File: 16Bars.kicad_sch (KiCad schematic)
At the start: 54 parts, among them IC1 CD4033BE, IC2 CD4033BE, IC3 CD4510BE, IC4 CD4510BE, IC5 CD4510BE, J1 3.5mm_Mono_Switched, J2 Conn_02x05_Odd_Even, Q1 2N3904, Q3 2N3904, Q4 2N3904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

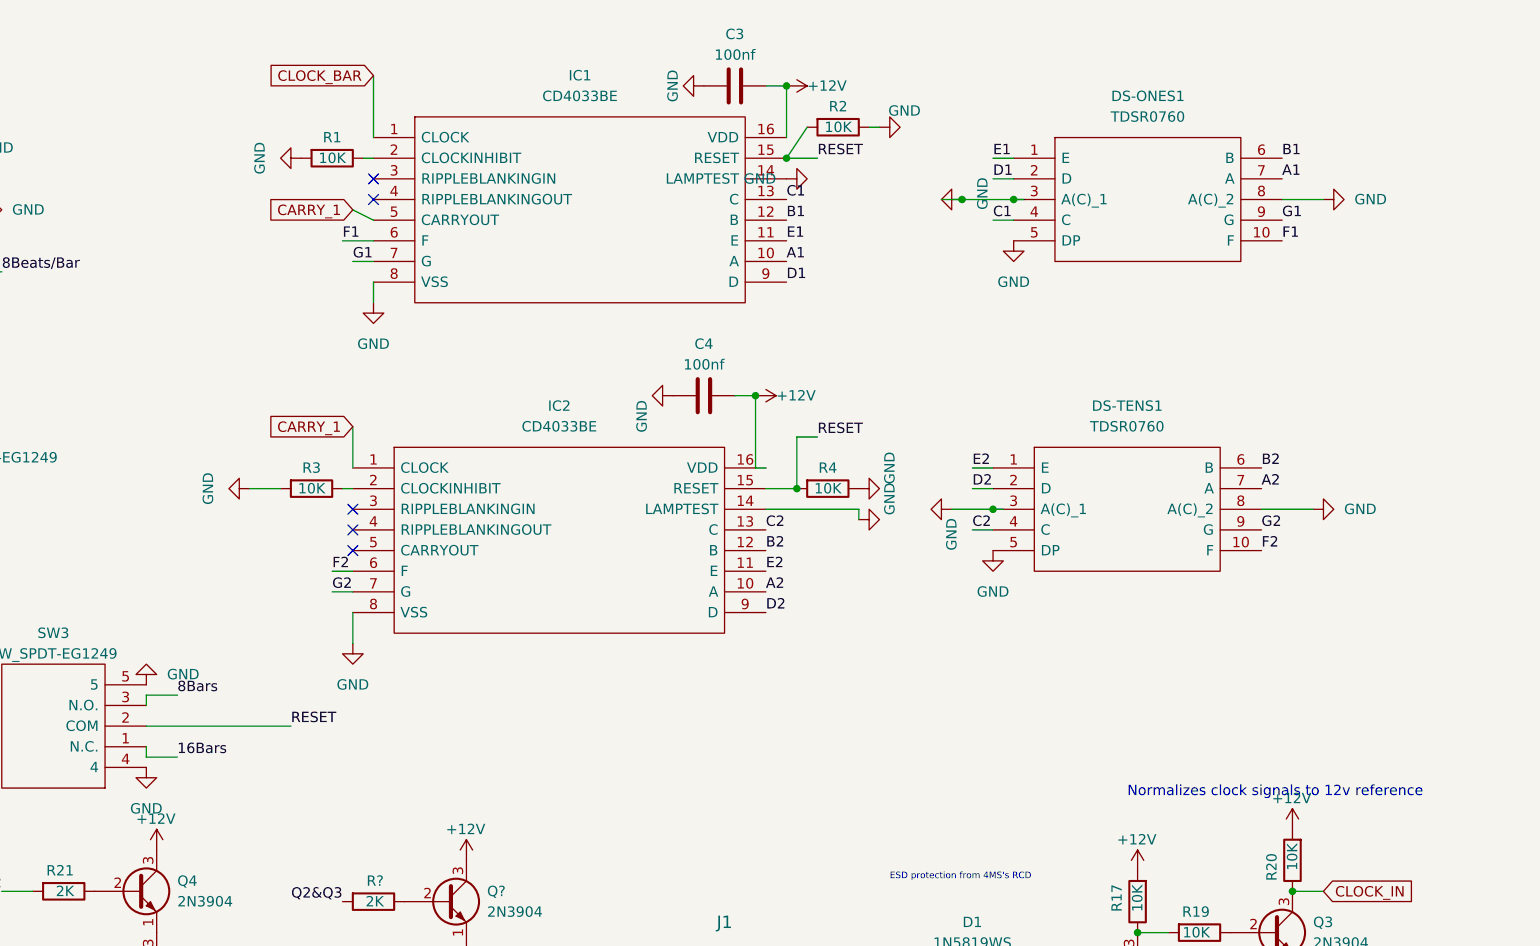
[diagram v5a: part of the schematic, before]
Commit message: Add SevenSegment sub-board
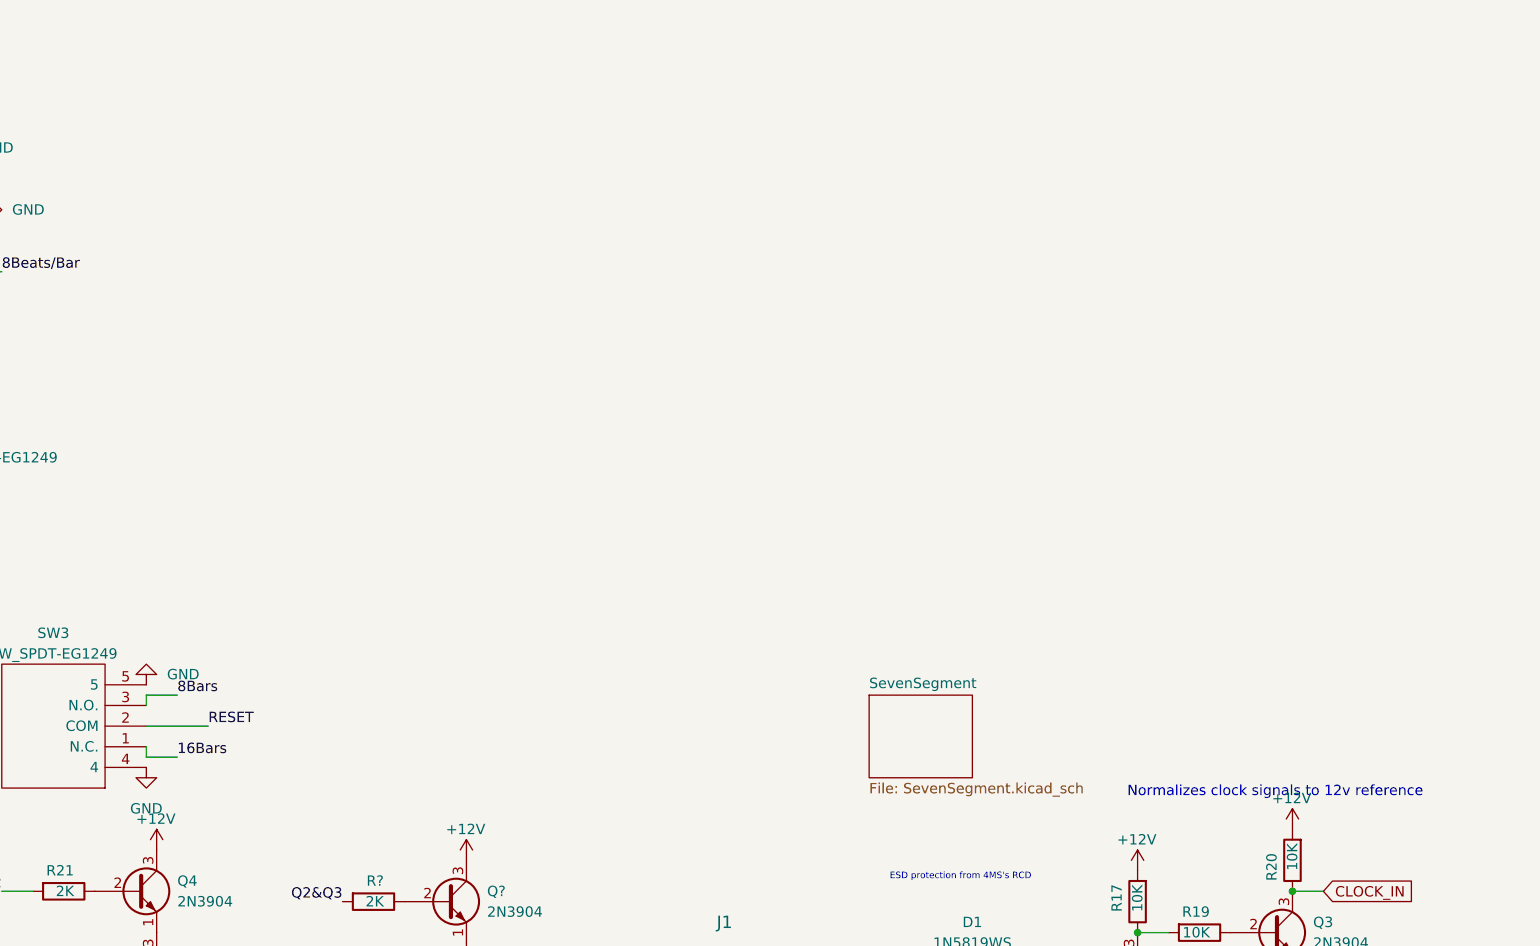
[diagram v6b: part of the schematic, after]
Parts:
- removed C3, C4: 100nf, Capacitor_SMD:C_0402_1005Metric, symbol Device:C
- removed DS-ONES1, DS-TENS1: TDSR0760, TDSR*:TDSR0760, symbol SamacSys_Parts:TDSR0760
- removed IC1, IC2: CD4033BE, DIP794W53P254L1930H508Q16N, symbol SamacSys_Parts:CD4033BE
- removed R1, R2, R3, R4: 10K, Resistor_SMD:R_0402_1005Metric, symbol Device:R
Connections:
- no-connect marks 12 -> 7
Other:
- added sheet SevenSegment (SevenSegment.kicad_sch)

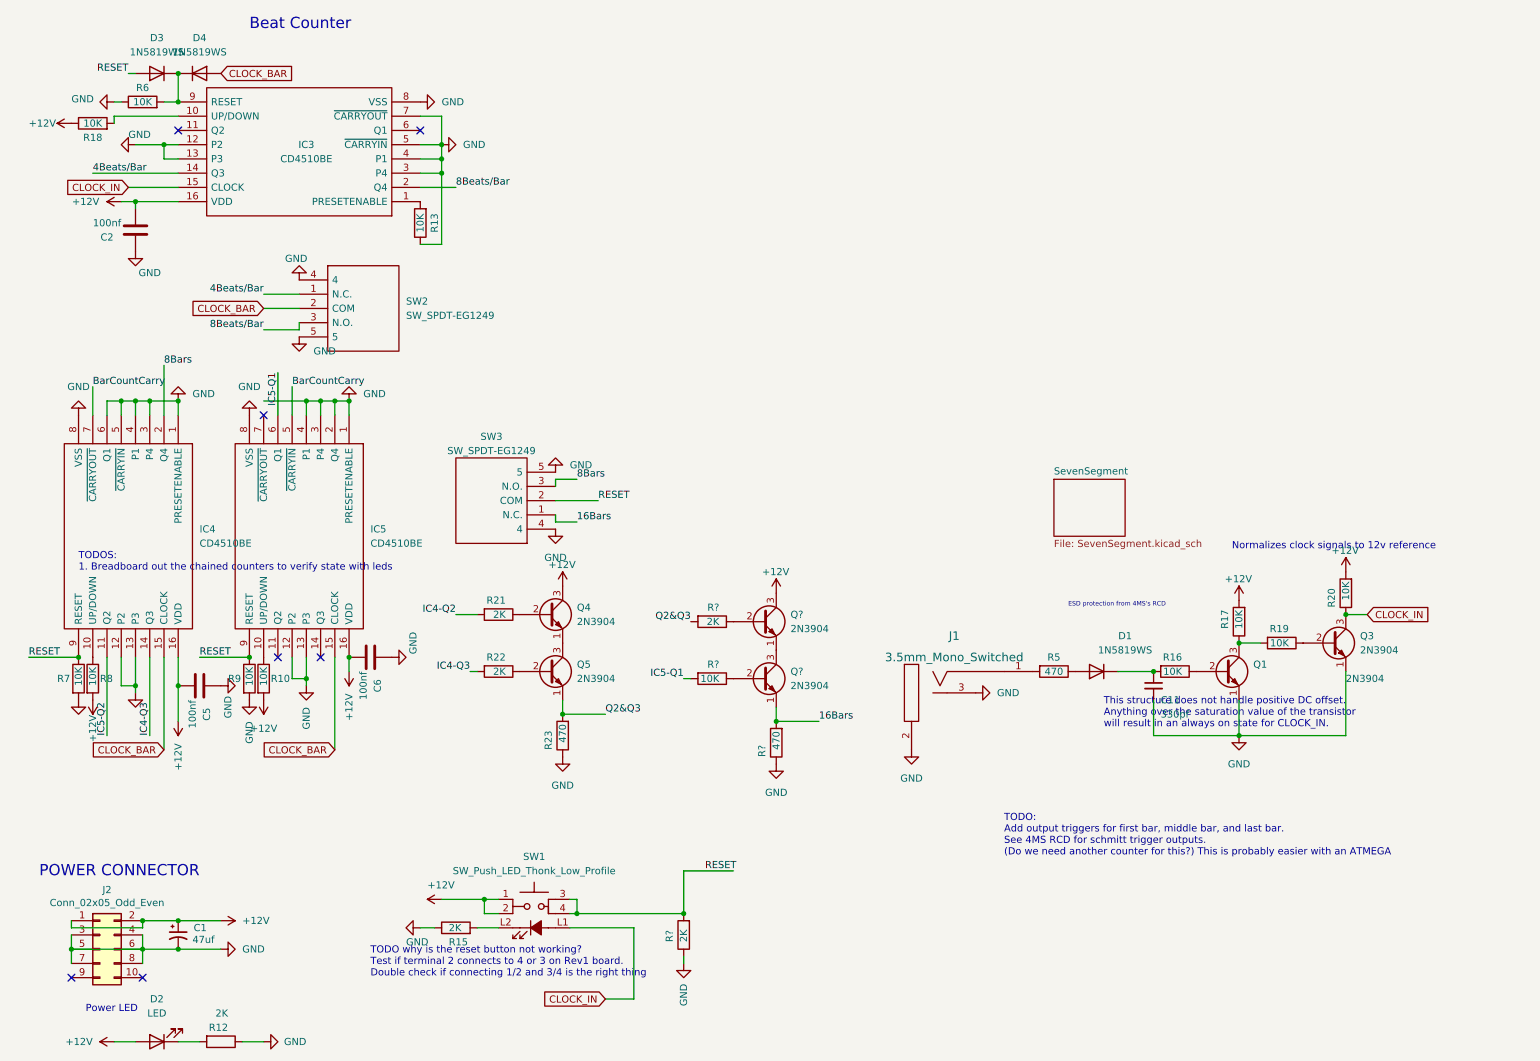
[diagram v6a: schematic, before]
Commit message: Layout SevenSegment Board. Nano Schematic
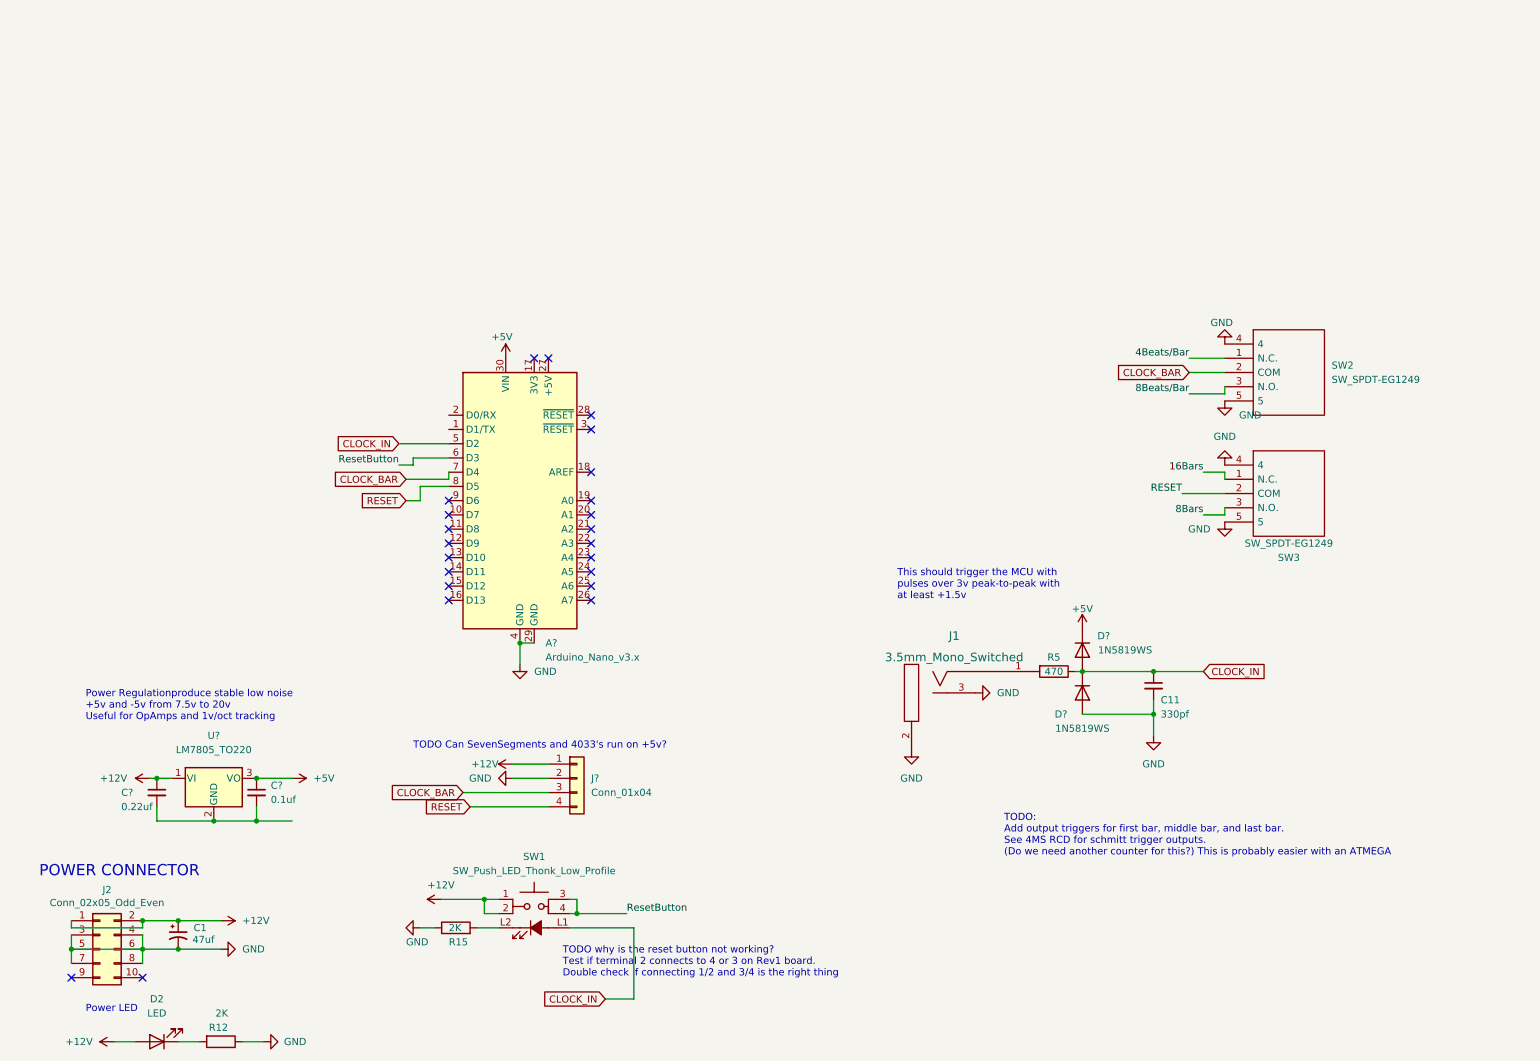
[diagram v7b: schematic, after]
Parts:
- removed C2, C5, C6: 100nf, Capacitor_SMD:C_0402_1005Metric, symbol Device:C
- removed D1, D3, D4: 1N5819WS, Diode_SMD:D_SOD-323, symbol Device:D
- removed IC3, IC4, IC5: CD4510BE, DIP794W53P254L1930H508Q16N, symbol SamacSys_Parts:CD4510BE
- removed Q1, Q3, Q4, Q5, Q? (x2): 2N3904, Package_TO_SOT_THT:TO-92_Inline, symbol Transistor_BJT:2N3904
- removed R10, R13, R16, R17, R18, R19, R20, R6, R7, R8, R9, R?: 10K, Resistor_SMD:R_0402_1005Metric, symbol Device:R
- removed R21, R22, R? (x2): 2K, Resistor_SMD:R_0402_1005Metric, symbol Device:R
- removed R23, R?: 470, Resistor_SMD:R_0402_1005Metric, symbol Device:R
- added A?: Arduino_Nano_v3.x, Module:Arduino_Nano, symbol MCU_Module:Arduino_Nano_v3.x
- added C?: 0.1uf, symbol Device:C_Small
- added C?: 0.22uf, symbol Device:C_Small
- added D? (x2): 1N5819WS, Diode_SMD:D_SOD-323, symbol Device:D
- added J?: Conn_01x04, 4ms_Connector:Pins_1x04_2.54mm_TH_SWD, symbol 4ms_Connector:Conn_01x04
- added U?: LM7805_TO220, Package_TO_SOT_THT:TO-220-3_Vertical, symbol Regulator_Linear:LM7805_TO220
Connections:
- net +12V: now also C?.1, J?.1 (Pin_1), U?.1 (VI)
- net CLOCK_BAR: now also A?.7 (D4), J?.3 (Pin_3)
- net CLOCK_IN: now also C11.1, R5.1, A?.5 (D2), D?.1 (K), D?.2 (A)
- net GND: now also A?.29 (GND), A?.4 (GND), D?.2 (A), J?.2 (Pin_2)
- net RESET: now also A?.8 (D5), J?.4 (Pin_4); no longer SW1.3, SW1.4
- new net: C?.2, C?.2, U?.2 (GND)
- new net +5V: A?.30 (VIN), C?.1, D?.1 (K), U?.3 (VO)
- new net ResetButton: A?.6 (D3), SW1.3, SW1.4
- no-connect marks 7 -> 23
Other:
- removed sheet SevenSegment
- note added: "Power Regulationproduce stable low noise +5v and -5v from 7.5v to 20v Useful for OpAmps and 1v/oct tracking"
- note added: "TODO Can SevenSegments and 4033's run on +5v?"
- note added: "This should trigger the MCU with pulses over 3v peak-to-peak with at least +1.5v"
- note removed: "Beat Counter"
- note removed: "ESD protection from 4MS's RCD"
- note removed: "Normalizes clock signals to 12v reference"
- note removed: "TODOS: 1. Breadboard out the chained counters to verify state with leds"
- note removed: "This structure does not handle positive DC offset. Anything over the saturation value of the transistor will result in an always on state for CLOCK_IN."
- moved on the sheet: SW2, SW3

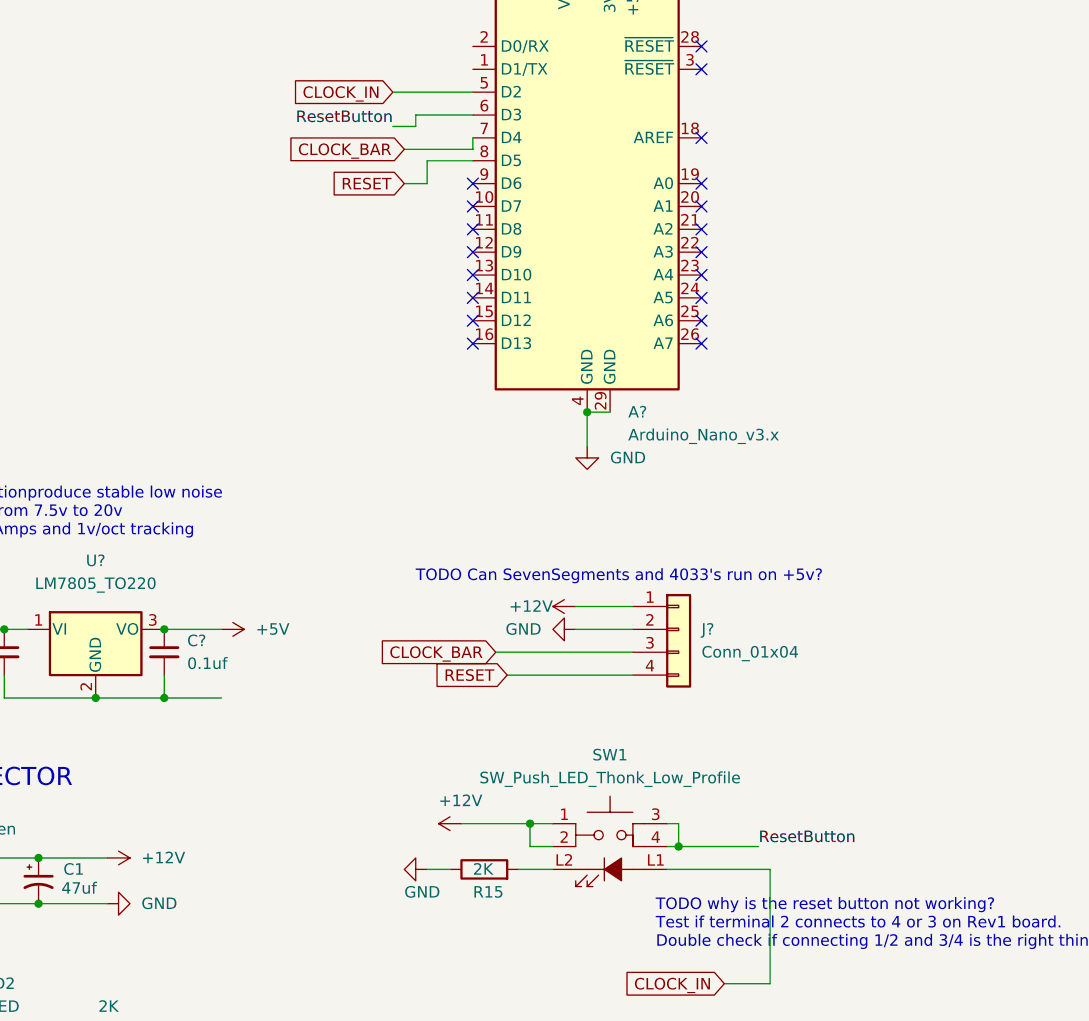
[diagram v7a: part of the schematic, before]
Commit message: Add LED output pins. Hookup pins in schematic.
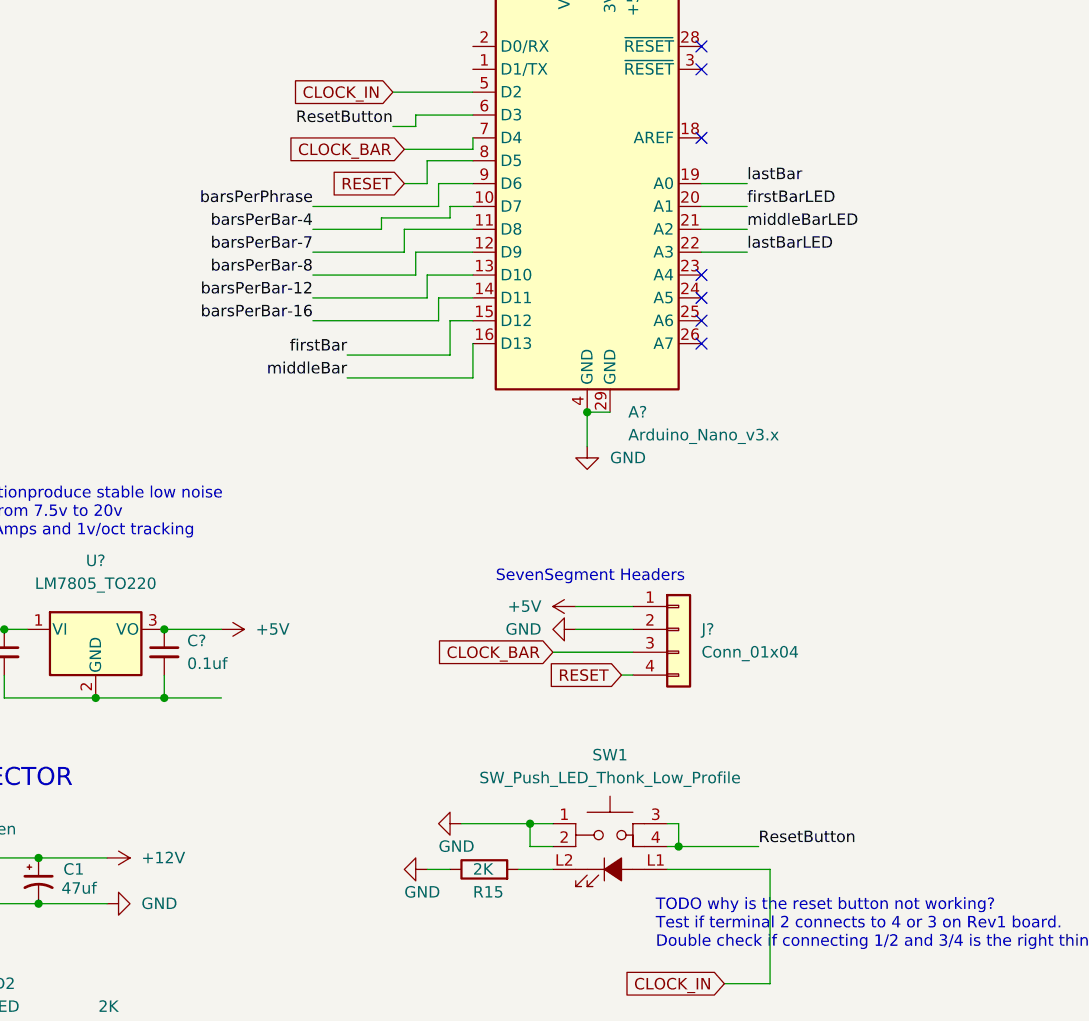
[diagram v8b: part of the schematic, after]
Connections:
- net +12V: no longer J?.1 (Pin_1), SW1.1, SW1.2
- net +5V: now also J?.1 (Pin_1)
- net GND: now also SW1.1, SW1.2
- net barsPerBar-4: now reaches A?.10 (D7)
- net barsPerBar-7: now reaches A?.11 (D8)
- net barsPerBar-8: now reaches A?.12 (D9)
- net barsPerBar-12: now reaches A?.13 (D10)
- net barsPerBar-16: now reaches A?.14 (D11)
- net firstBar: now reaches A?.15 (D12)
- net middleBar: now reaches A?.16 (D13)
- net lastBar: now reaches A?.19 (A0)
- net firstBarLED: now reaches A?.20 (A1)
- net middleBarLED: now reaches A?.21 (A2)
- net lastBarLED: now reaches A?.22 (A3)
- net barsPerPhrase: now reaches A?.9 (D6)
- no-connect marks 23 -> 11
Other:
- note added: "SevenSegment Headers"
- note removed: "TODO Can SevenSegments and 4033's run on +5v?"
